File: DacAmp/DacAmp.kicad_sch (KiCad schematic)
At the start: 0 parts

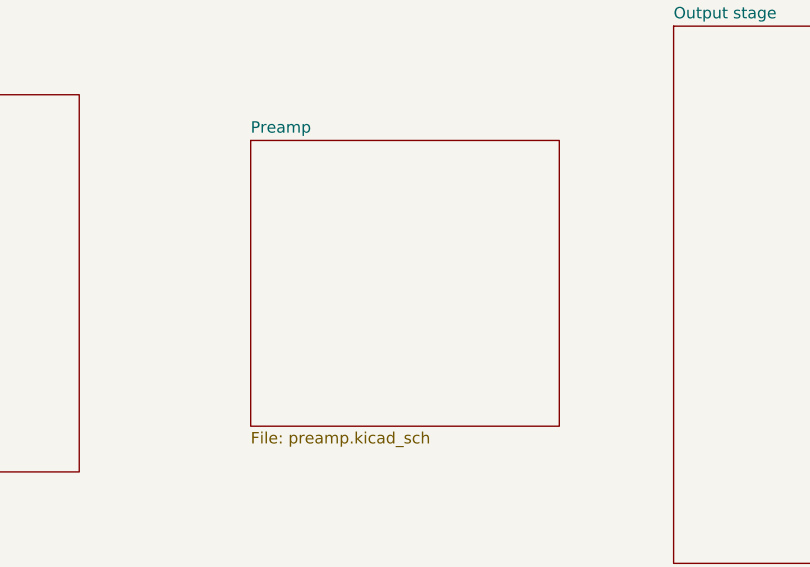
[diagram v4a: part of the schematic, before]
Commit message: complete overall schematic, TODO: find values and add net labels
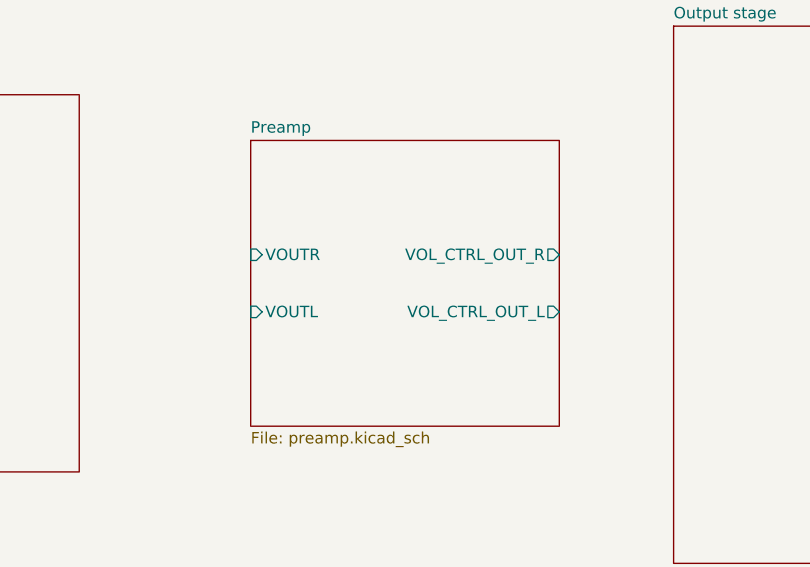
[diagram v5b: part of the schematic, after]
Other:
- sheet Preamp ports: added VOL_CTRL_OUT_L, VOL_CTRL_OUT_R, VOUTL, VOUTR; removed none
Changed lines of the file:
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@@
+			)
+		)
+		(pin "VOUTL" input
+			(at 173.99 106.68 180)
+			(effects
+				(font
+					(size 1.27 1.27)
+				)
+				(justify left)
+			)
+		)
+		(pin "VOUTR" input
+			(at 173.99 100.33 180)
+			(effects
+				(font
+					(size 1.27 1.27)
+				)
+				(justify left)
+			)
+		)
+		(pin "VOL_CTRL_OUT_R" output
+			(at 208.28 100.33 0)
+			(effects
+				(font
+					(size 1.27 1.27)
+				)
+				(justify right)
+			)
+		)
+		(pin "VOL_CTRL_OUT_L" output
+			(at 208.28 106.68 0)
+			(effects
+				(font
+					(size 1.27 1.27)
+				)
+				(justify right)
 			)
 		)

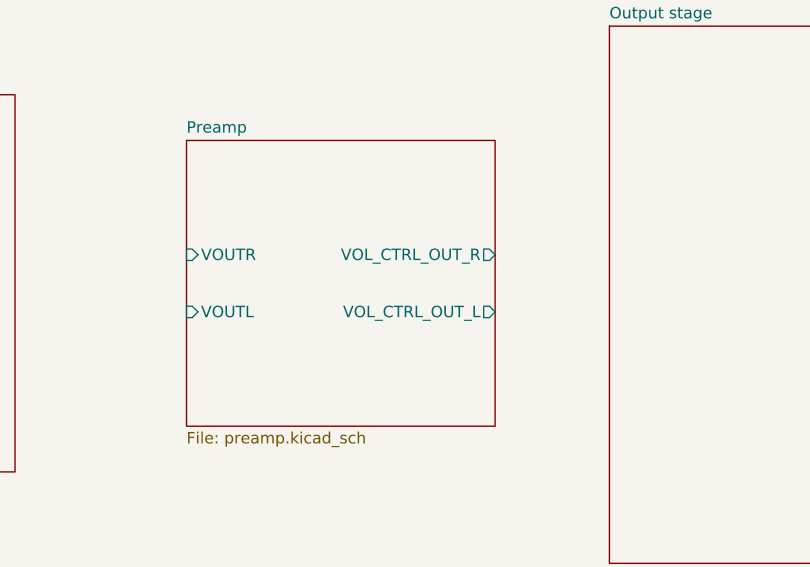
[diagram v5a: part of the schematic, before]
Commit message: added phase reversal to volume control stage
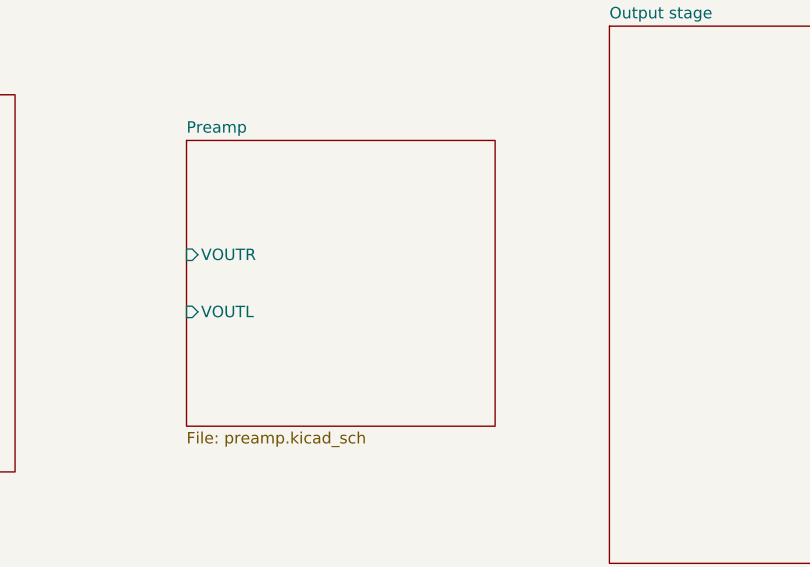
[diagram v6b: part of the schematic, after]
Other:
- sheet Preamp ports: added none; removed VOL_CTRL_OUT_L, VOL_CTRL_OUT_R
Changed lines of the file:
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@@
-			)
-		)
-		(pin "VOL_CTRL_OUT_R" output
-			(at 208.28 100.33 0)
-			(effects
-				(font
-					(size 1.27 1.27)
-				)
-				(justify right)
-			)
-		)
-		(pin "VOL_CTRL_OUT_L" output
-			(at 208.28 106.68 0)
-			(effects
-				(font
-					(size 1.27 1.27)
-				)
-				(justify right)
 			)
 		)

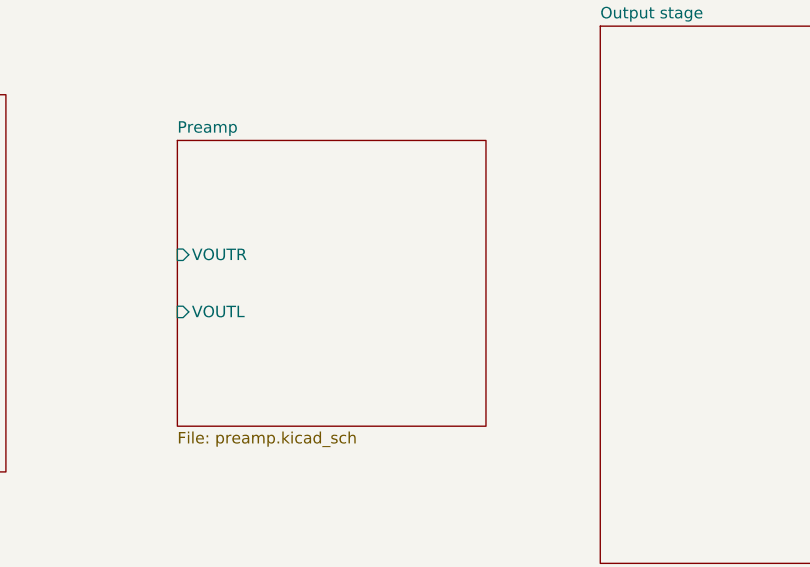
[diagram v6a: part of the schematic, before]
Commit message: make preamp diagram block-y
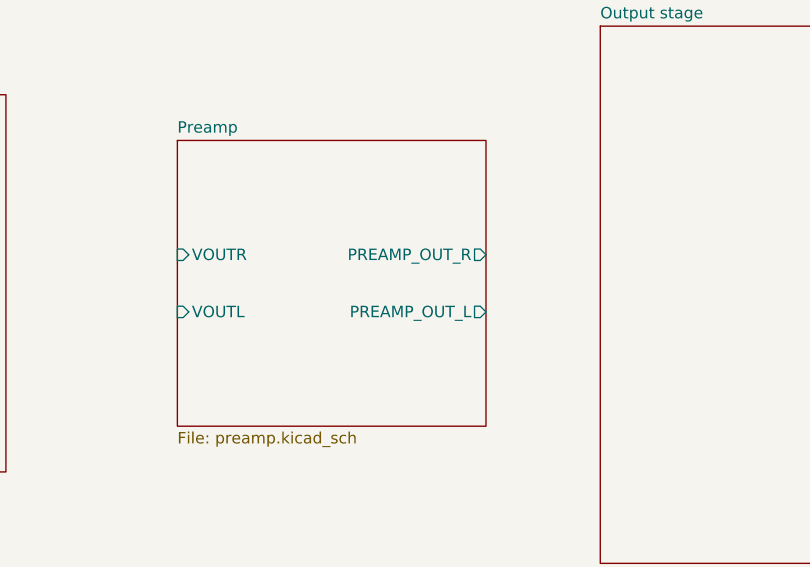
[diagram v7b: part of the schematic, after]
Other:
- sheet Preamp ports: added PREAMP_OUT_L, PREAMP_OUT_R; removed none
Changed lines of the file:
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@@
+			)
+		)
+		(pin "PREAMP_OUT_R" output
+			(at 208.28 100.33 0)
+			(effects
+				(font
+					(size 1.27 1.27)
+				)
+				(justify right)
+			)
+		)
+		(pin "PREAMP_OUT_L" output
+			(at 208.28 106.68 0)
+			(effects
+				(font
+					(size 1.27 1.27)
+				)
+				(justify right)
 			)
 		)

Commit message: start some layout
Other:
- sheet Codec ports: added CONN_D+, CONN_D-, VOUTL, VOUTR; removed none
- sheet Output stage ports: added PREAMP_OUT_L, PREAMP_OUT_R; removed none
- sheet USB ports: added CONN_D+, CONN_D-; removed none
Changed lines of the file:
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@@
 	(generator_version "8.0")
 	(paper "A4")
+	(wire
+		(pts
+			(xy 85.09 105.41) (xy 113.03 105.41)
+		)
+		(stroke
+			(width 0)
+			(type default)
+		)
+	)
+	(wire
+		(pts
+			(xy 208.28 106.68) (xy 220.98 106.68)
+		)
+		(stroke
+			(width 0)
+			(type default)
+		)
+	)
+	(wire
+		(pts
+			(xy 154.94 106.68) (xy 173.99 106.68)
+		)
+		(stroke
+			(width 0)
+			(type default)
+		)
+	)
+	(wire
+		(pts
+			(xy 154.94 100.33) (xy 173.99 100.33)
+		)
+		(stroke
+			(width 0)
+			(type default)
+		)
+	)
+	(wire
+		(pts
+			(xy 85.09 102.87) (xy 113.03 102.87)
+		)
+		(stroke
+			(width 0)
+			(type default)
+		)
+	)
+	(wire
+		(pts
+			(xy 208.28 100.33) (xy 220.98 100.33)
+		)
+		(stroke
+			(width 0)
+			(type default)
+		)
+	)
 	(text "Idea: \nMake selectable voltage output? Like if youre driving earbuds you're not gonna want higher rms voltage over the thing."
 		(exclude_from_sim no)
@@
 			)
 		)
+		(pin "PREAMP_OUT_L" input
+			(at 220.98 106.68 180)
+			(effects
+				(font
+					(size 1.27 1.27)
+				)
+				(justify left)
+			)
+		)
+		(pin "PREAMP_OUT_R" input
+			(at 220.98 100.33 180)
+			(effects
+				(font
+					(size 1.27 1.27)
+				)
+				(justify left)
+			)
+		)
 		(instances
 			(project "DacAmp"
@@
 			)
 		)
+		(pin "CONN_D-" output
+			(at 85.09 105.41 0)
+			(effects
+				(font
+					(size 1.27 1.27)
+				)
+				(justify right)
+			)
+		)
+		(pin "CONN_D+" output
+			(at 85.09 102.87 0)
+			(effects
+				(font
+					(size 1.27 1.27)
+				)
+				(justify right)
+			)
+		)
 		(instances
 			(project "DacAmp"
@@
 			)
 		)
+		(pin "VOUTL" output
+			(at 154.94 106.68 0)
+			(effects
+				(font
+					(size 1.27 1.27)
+				)
+				(justify right)
+			)
+		)
+		(pin "VOUTR" output
+			(at 154.94 100.33 0)
+			(effects
+				(font
+					(size 1.27 1.27)
+				)
+				(justify right)
+			)
+		)
+		(pin "CONN_D-" input
+			(at 113.03 105.41 180)
+			(effects
+				(font
+					(size 1.27 1.27)
+				)
+				(justify left)
+			)
+		)
+		(pin "CONN_D+" input
+			(at 113.03 102.87 180)
+			(effects
+				(font
+					(size 1.27 1.27)
+				)
+				(justify left)
+			)
+		)
